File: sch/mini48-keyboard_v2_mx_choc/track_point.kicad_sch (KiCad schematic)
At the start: 23 parts, among them J1 Conn_01x08, Q1 BSS138, Q2 BSS138, Q3 BSS138, SW100 SW_Push, SW101 SW_Push, SW102 SW_Push, SW97 SW_Push, SW98 SW_Push, SW99 SW_Push

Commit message: シンボルパス、フットプリントパスを修正しました。 基板製造に使用したファイルを追加しました。
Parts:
- J1: footprint Connector_JST:JST_PH_B8B-PH-K_1x08_P2.00mm_Vertical -> Connector_JST:JST_XH_B8B-XH-A_1x08_P2.50mm_Vertical
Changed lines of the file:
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@@
 			)
 		)
-		(property "Footprint" "Connector_JST:JST_PH_B8B-PH-K_1x08_P2.00mm_Vertical"
+		(property "Footprint" "Connector_JST:JST_XH_B8B-XH-A_1x08_P2.50mm_Vertical"
 			(at 196.85 83.82 0)
 			(effects

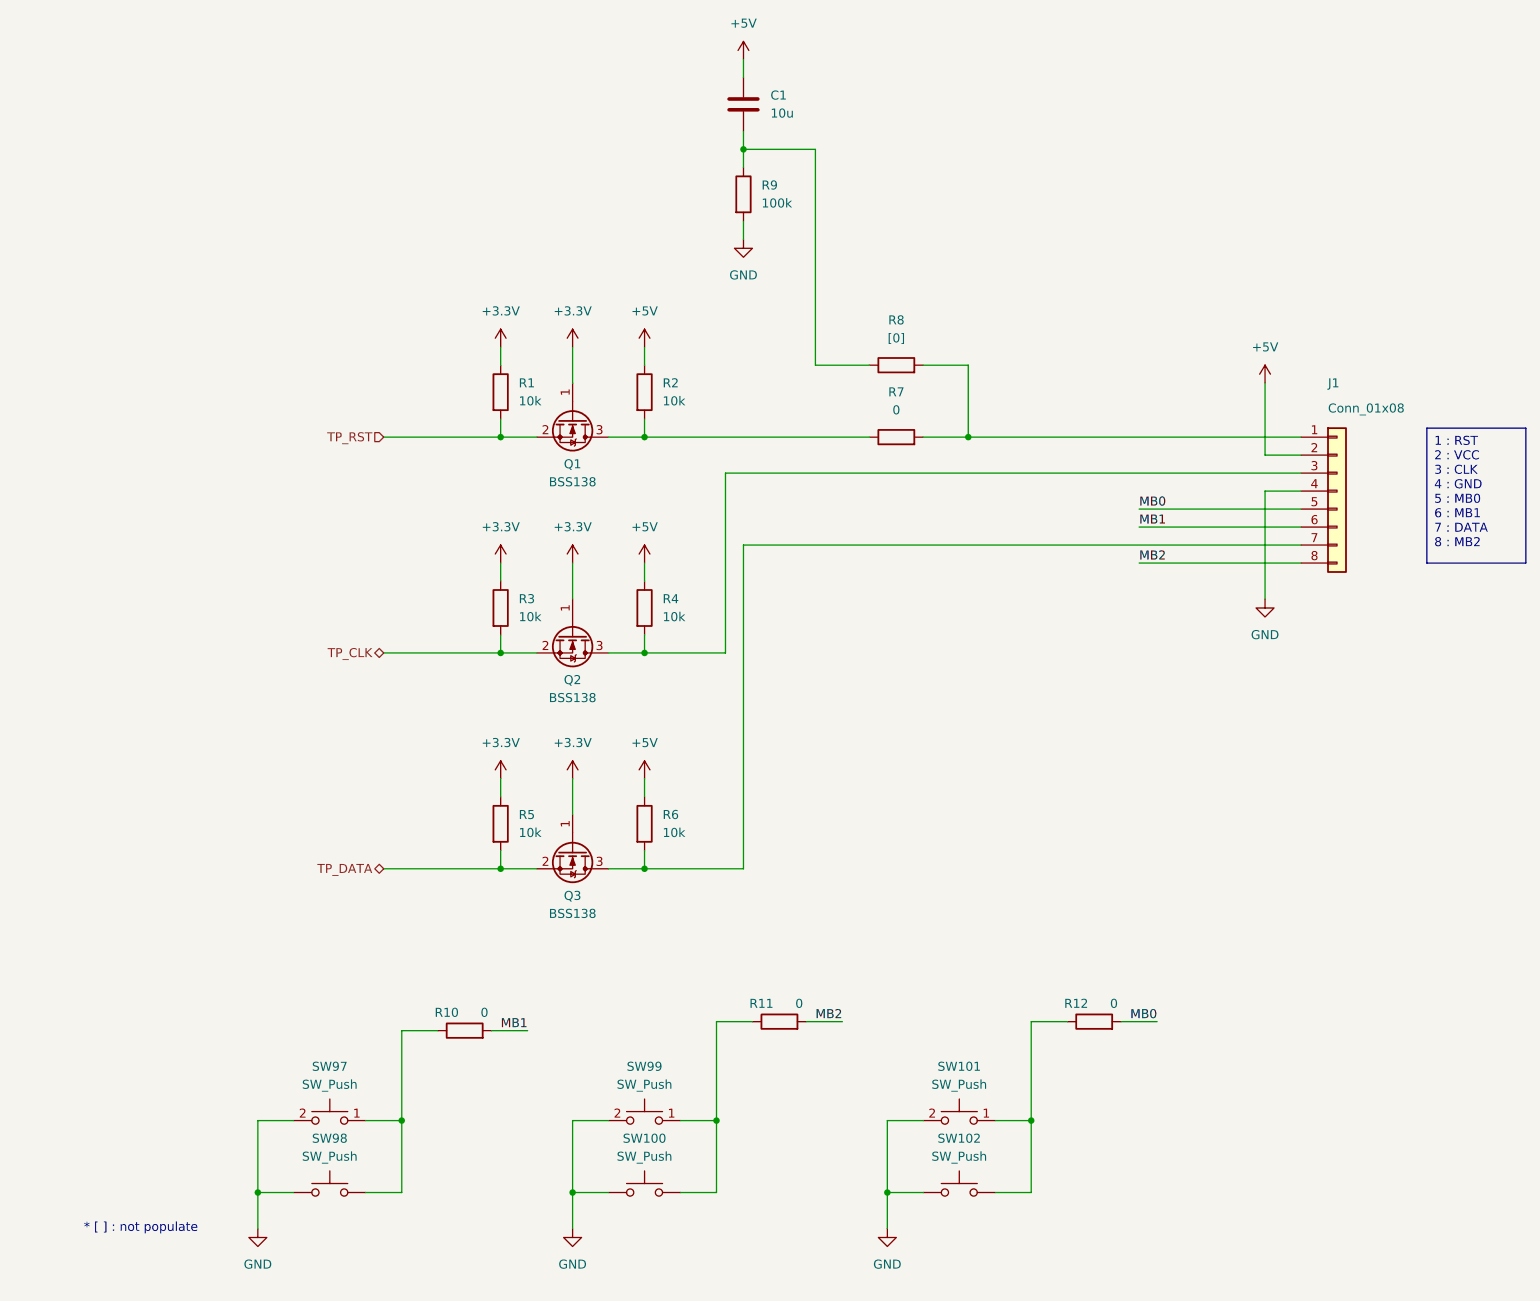
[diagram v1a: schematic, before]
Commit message: やっぱり標準のマイコンはpicoのピン配に合わせる。
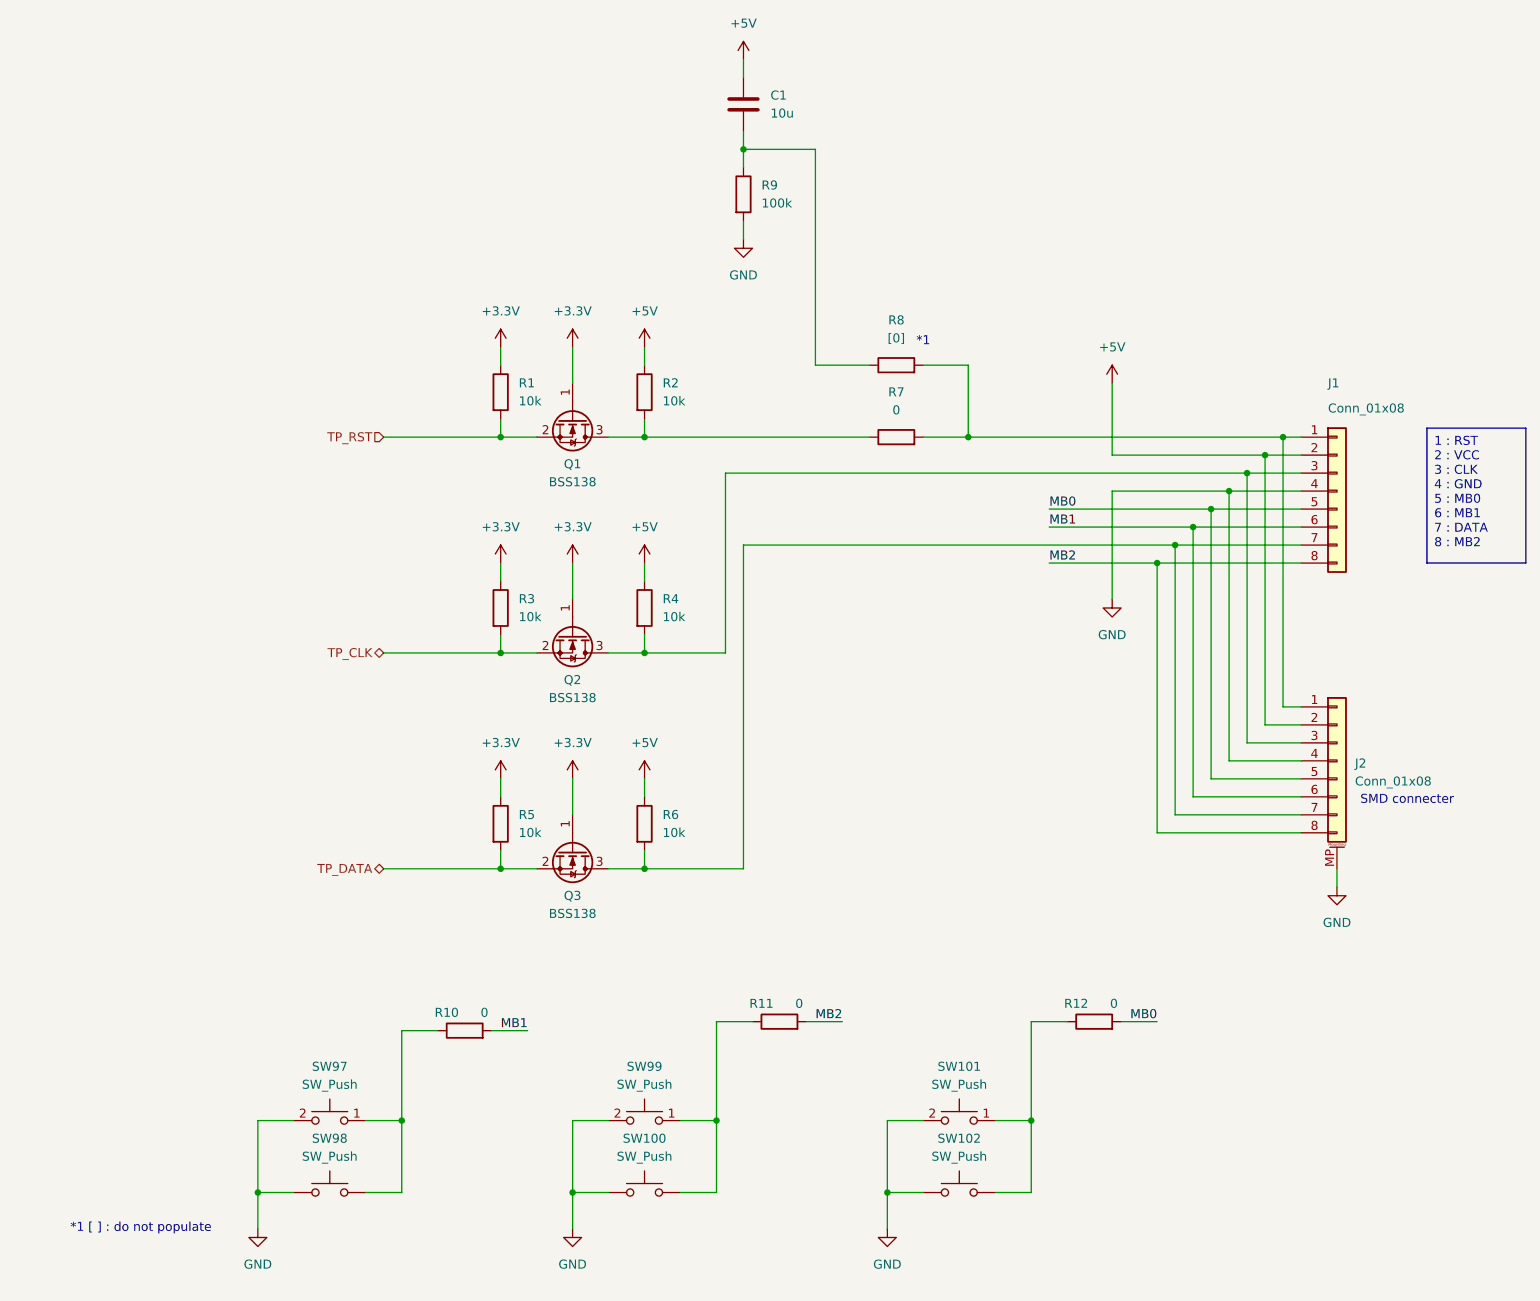
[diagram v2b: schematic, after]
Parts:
- added J2: Conn_01x08, Connector_Hirose:Hirose_DF13C_CL535-0408-9-51_1x08-1MP_P1.25mm_Vertical, symbol Connector_Generic_MountingPin:Conn_01x08_MountingPin
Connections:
- net +5V: now also J2.2 (Pin_2)
- net GND: now also J2.4 (Pin_4), J2.MP (MountPin)
- net MB0: now also J2.5 (Pin_5)
- net MB1: now also J2.6 (Pin_6)
- net MB2: now also J2.8 (Pin_8)
- net at J1.3 (Pin_3), Q2.3 (D), R4.2: now also J2.3 (Pin_3)
- net at J1.1 (Pin_1), R7.2, R8.2: now also J2.1 (Pin_1)
- net at J1.7 (Pin_7), Q3.3 (D), R6.2: now also J2.7 (Pin_7)
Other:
- note added: "*1"
- note added: "*1 [ ] : do not populate"
- note added: "SMD connecter"
- note removed: "* [ ] : not populate"

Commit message: ひとまずすべての未配線をなくした版です。 配線は整えていません。 また、GNDプレーンのビアは打っていません。
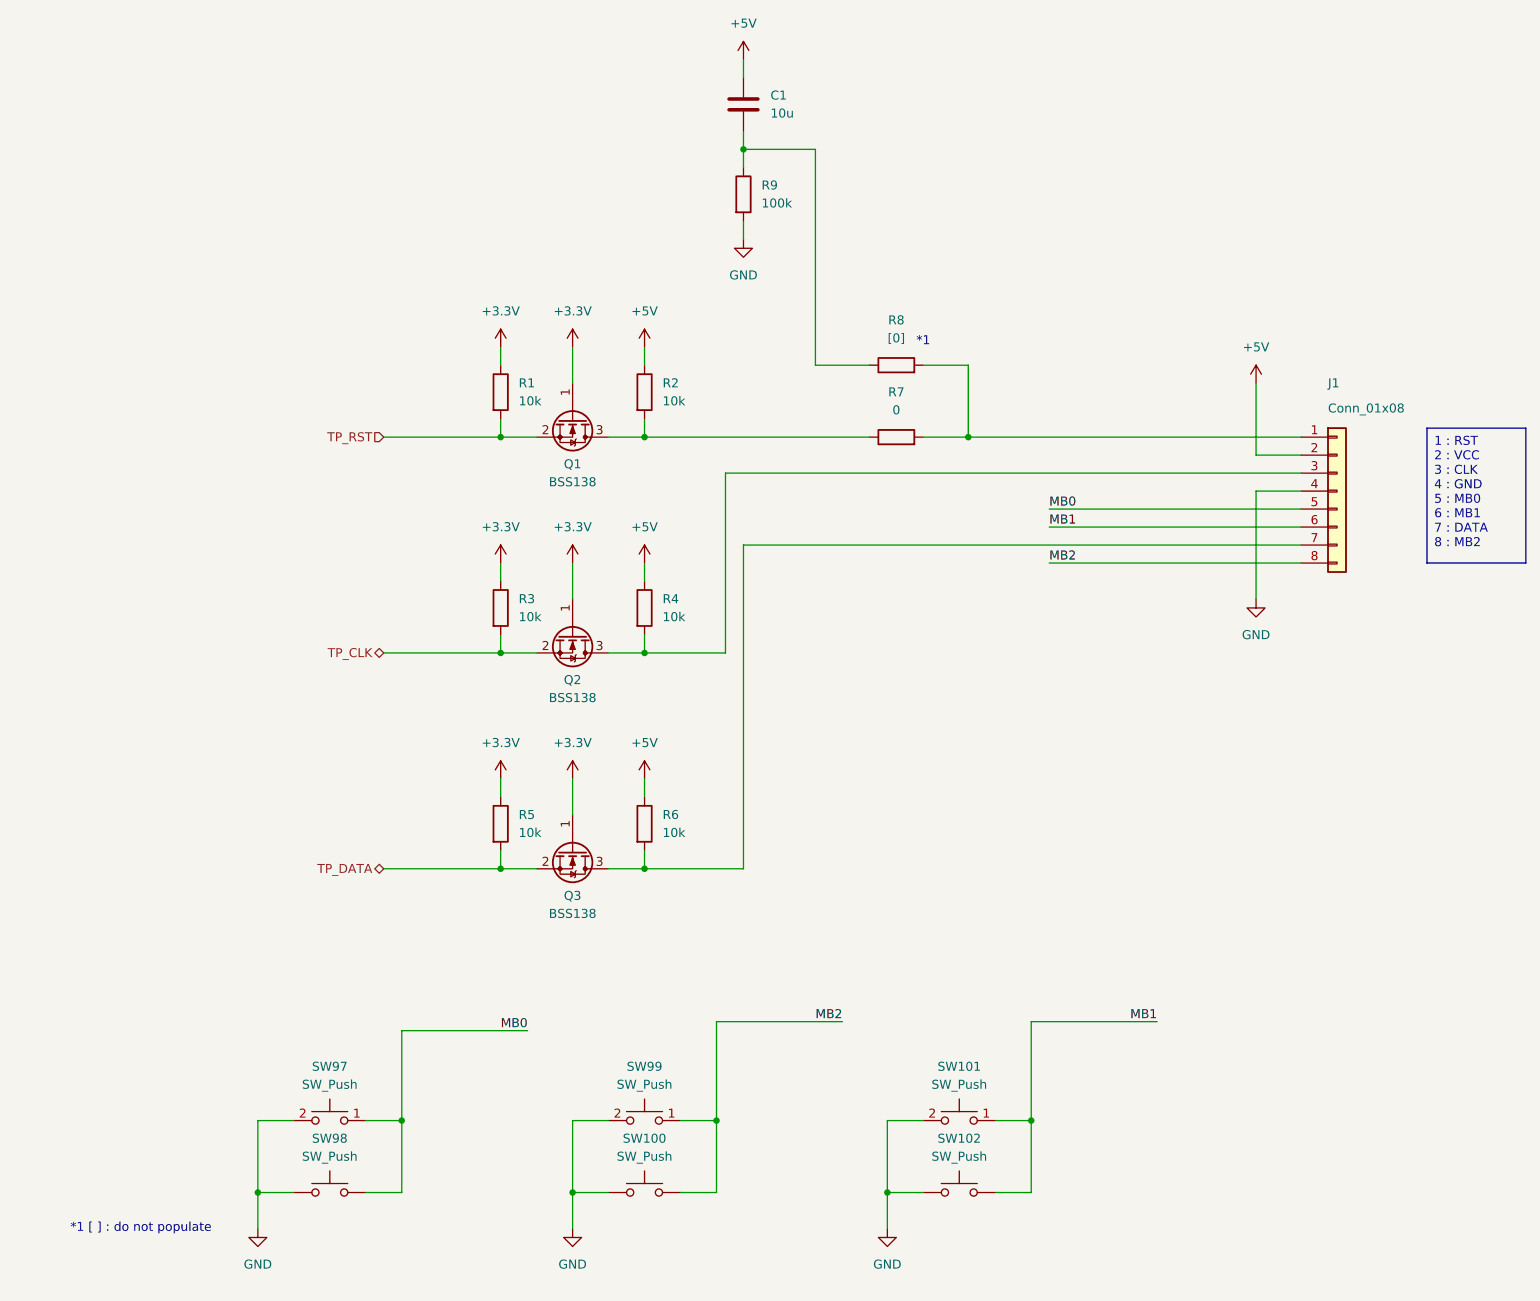
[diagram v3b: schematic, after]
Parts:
- removed J2: Conn_01x08, Connector_Hirose:Hirose_DF13C_CL535-0408-9-51_1x08-1MP_P1.25mm_Vertical, symbol Connector_Generic_MountingPin:Conn_01x08_MountingPin
- removed R10, R11, R12: 0, Resistor_SMD:R_0603_1608Metric, symbol Device:R
- J1: footprint Connector_JST:JST_XH_B8B-XH-A_1x08_P2.50mm_Vertical -> Connector_JST:JST_XH_S8B-XH-A_1x08_P2.50mm_Horizontal
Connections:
- net MB0: now also SW97.1, SW98.2
- net MB1: now also SW101.1, SW102.2
- net MB2: now also SW100.2, SW99.1
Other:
- note removed: "SMD connecter"

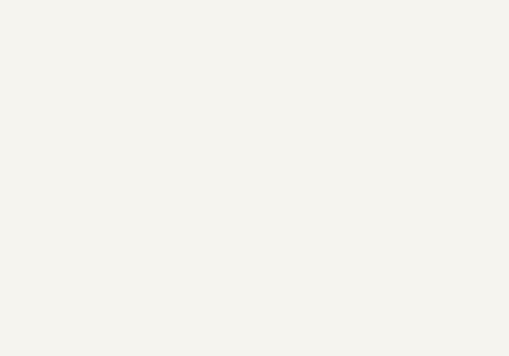
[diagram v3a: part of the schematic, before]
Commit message: トラックポイント(2ピースタイプ)の取り付けステーです。 トラックポイントの軸の延長部品です。
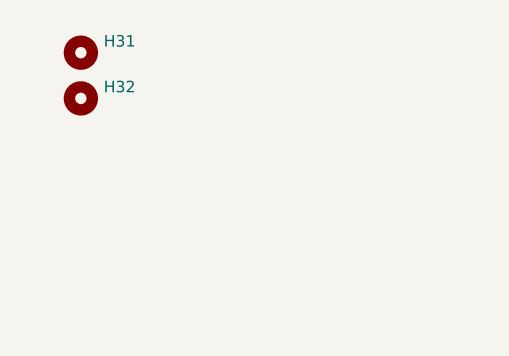
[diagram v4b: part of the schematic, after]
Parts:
- added H31, H32: MountingHole, MountingHole:MountingHole_2.2mm_M2, symbol Mechanical:MountingHole
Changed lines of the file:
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@@
+	)
+	(symbol
+		(lib_id "Mechanical:MountingHole")
+		(at 20.32 25.4 0)
+		(unit 1)
+		(exclude_from_sim yes)
+		(in_bom no)
+		(on_board yes)
+		(dnp no)
+		(fields_autoplaced yes)
+		(property "Reference" "H32"
+			(at 22.86 24.1299 0)
+			(effects
+				(font
+					(size 1.27 1.27)
+				)
+				(justify left)
+			)
+		)
+		(property "Value" "MountingHole"
+			(at 22.86 26.6699 0)
+			(effects
+				(font
+					(size 1.27 1.27)
+				)
+				(justify left)
+				(hide yes)
+			)
+		)
+		(property "Footprint" "MountingHole:MountingHole_2.2mm_M2"
+			(at 20.32 25.4 0)
+			(effects
+				(font
+					(size 1.27 1.27)
+				)
+				(hide yes)
+			)
+		)
+		(property "Datasheet" "~"
+			(at 20.32 25.4 0)
+			(effects
+				(font
+					(size 1.27 1.27)
+				)
+				(hide yes)
+			)
+		)
+		(property "Description" "Mounting Hole without connection"
+			(at 20.32 25.4 0)
+			(effects
+				(font
+					(size 1.27 1.27)
+				)
+				(hide yes)
+			)
+		)
+		(instances
+			(project "mini48-keyboard_v2_mx_choc"
+				(path "/c7705321-b11d-4074-930b-69ce3166659a/ce7a1281-26ab-4806-a94f-6cc7b3cf7456"
+					(reference "H32")
+					(unit 1)
+				)
+			)
+		)
 	)
 	(symbol
@@
 					(unit 1)
 				)
+			)
+		)
+	)
+	(symbol
+		(lib_id "Mechanical:MountingHole")
+		(at 20.32 20.32 0)
+		(unit 1)
+		(exclude_from_sim yes)
+		(in_bom no)
+		(on_board yes)
+		(dnp no)
+		(fields_autoplaced yes)
+		(property "Reference" "H31"
+			(at 22.86 19.0499 0)
+			(effects
+				(font
+					(size 1.27 1.27)
+				)
+				(justify left)
+			)
+		)
+		(property "Value" "MountingHole"
+			(at 22.86 21.5899 0)
+			(effects
+				(font
+					(size 1.27 1.27)
+				)
+				(justify left)
+				(hide yes)
+			)
+		)
+		(property "Footprint" "MountingHole:MountingHole_2.2mm_M2"
+			(at 20.32 20.32 0)
+			(effects
+				(font
+					(size 1.27 1.27)
+				)
+				(hide yes)
+			)
+		)
+		(property "Datasheet" "~"
+			(at 20.32 20.32 0)
+			(effects
+				(font
+					(size 1.27 1.27)
+				)
+				(hide yes)
+			)
+		)
+		(property "Description" "Mounting Hole without connection"
+			(at 20.32 20.32 0)
+			(effects
+				(font
+					(size 1.27 1.27)
+				)
+				(hide yes)
+			)
+		)
+		(instances
+			(project ""
+				(path "/c7705321-b11d-4074-930b-69ce3166659a/ce7a1281-26ab-4806-a94f-6cc7b3cf7456"
+					(reference "H31")
+					(unit 1)
+				)
